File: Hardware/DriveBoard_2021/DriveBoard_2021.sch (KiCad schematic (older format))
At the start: 66 parts, among them SW1 SW_Push, SW2 SW_Push, SW3 SW_Push, SW4 SW_Push, SW5 SW_Push, SW6 SW_Push, U1 TM4C129E_Launchpad, U2 LM2576S-3.3, U3 LM2576HVS-5, U4 MCP2551-I-SN

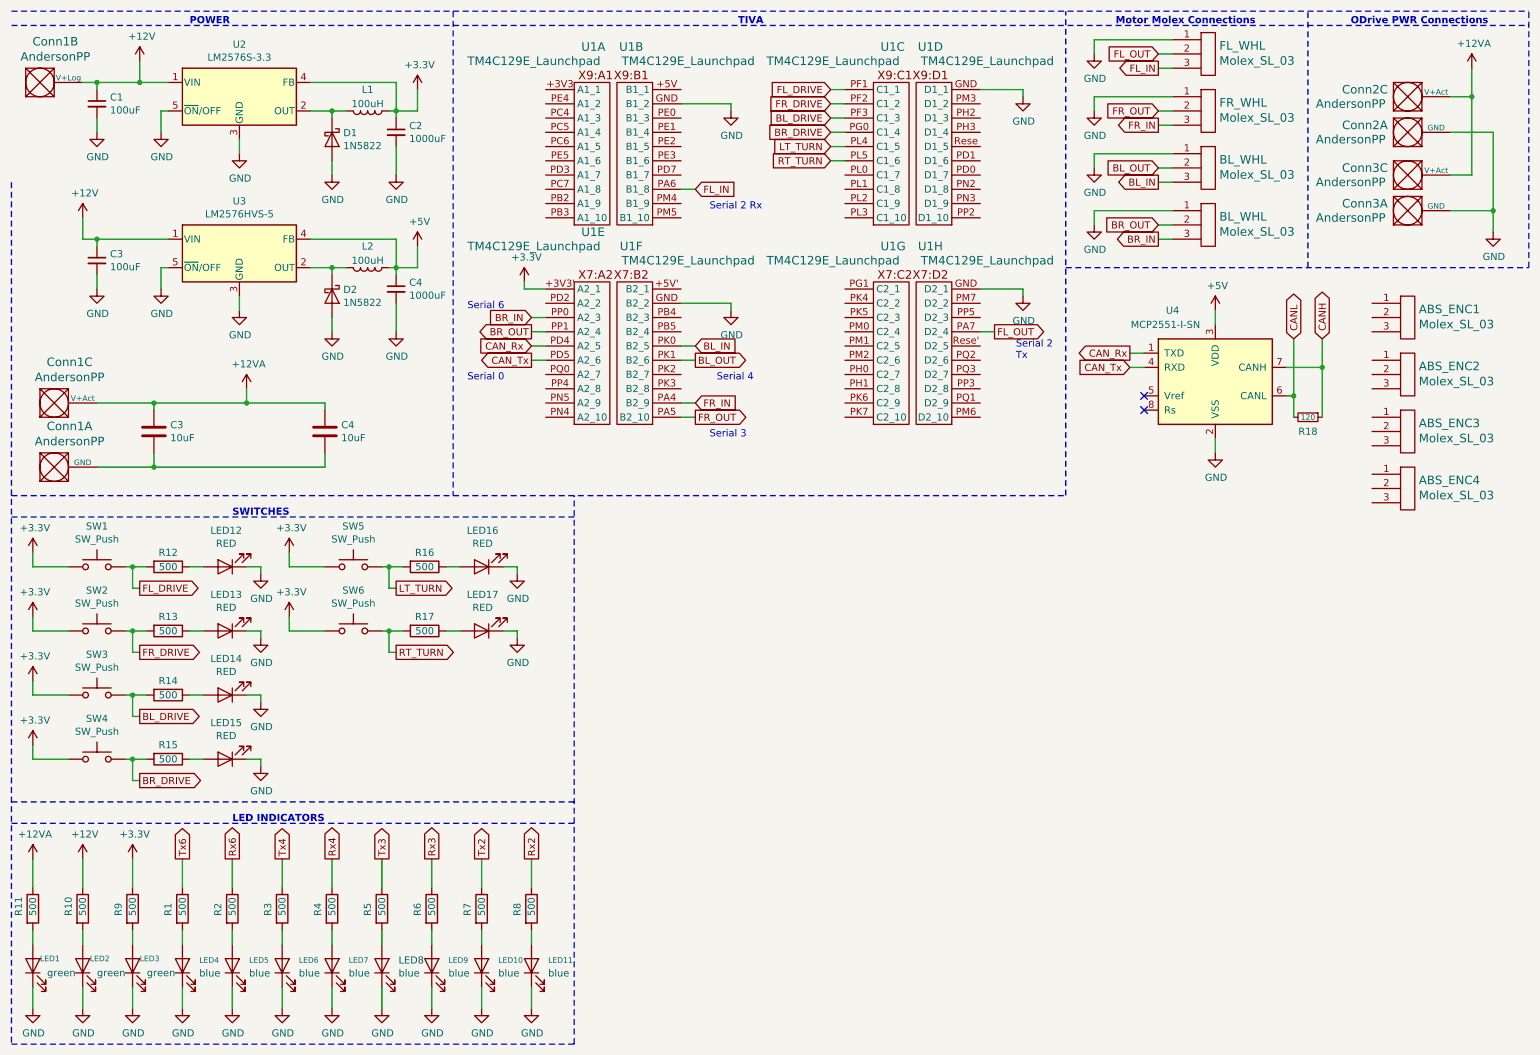
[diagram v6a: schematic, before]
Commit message: Added ODrive Serial, Added LED Indicators, Changed Serial Naming
Changed serial naming for easier understanding of pinout. Added LED indicators for 5V line, CAN serial, and both ODrive serial connections.
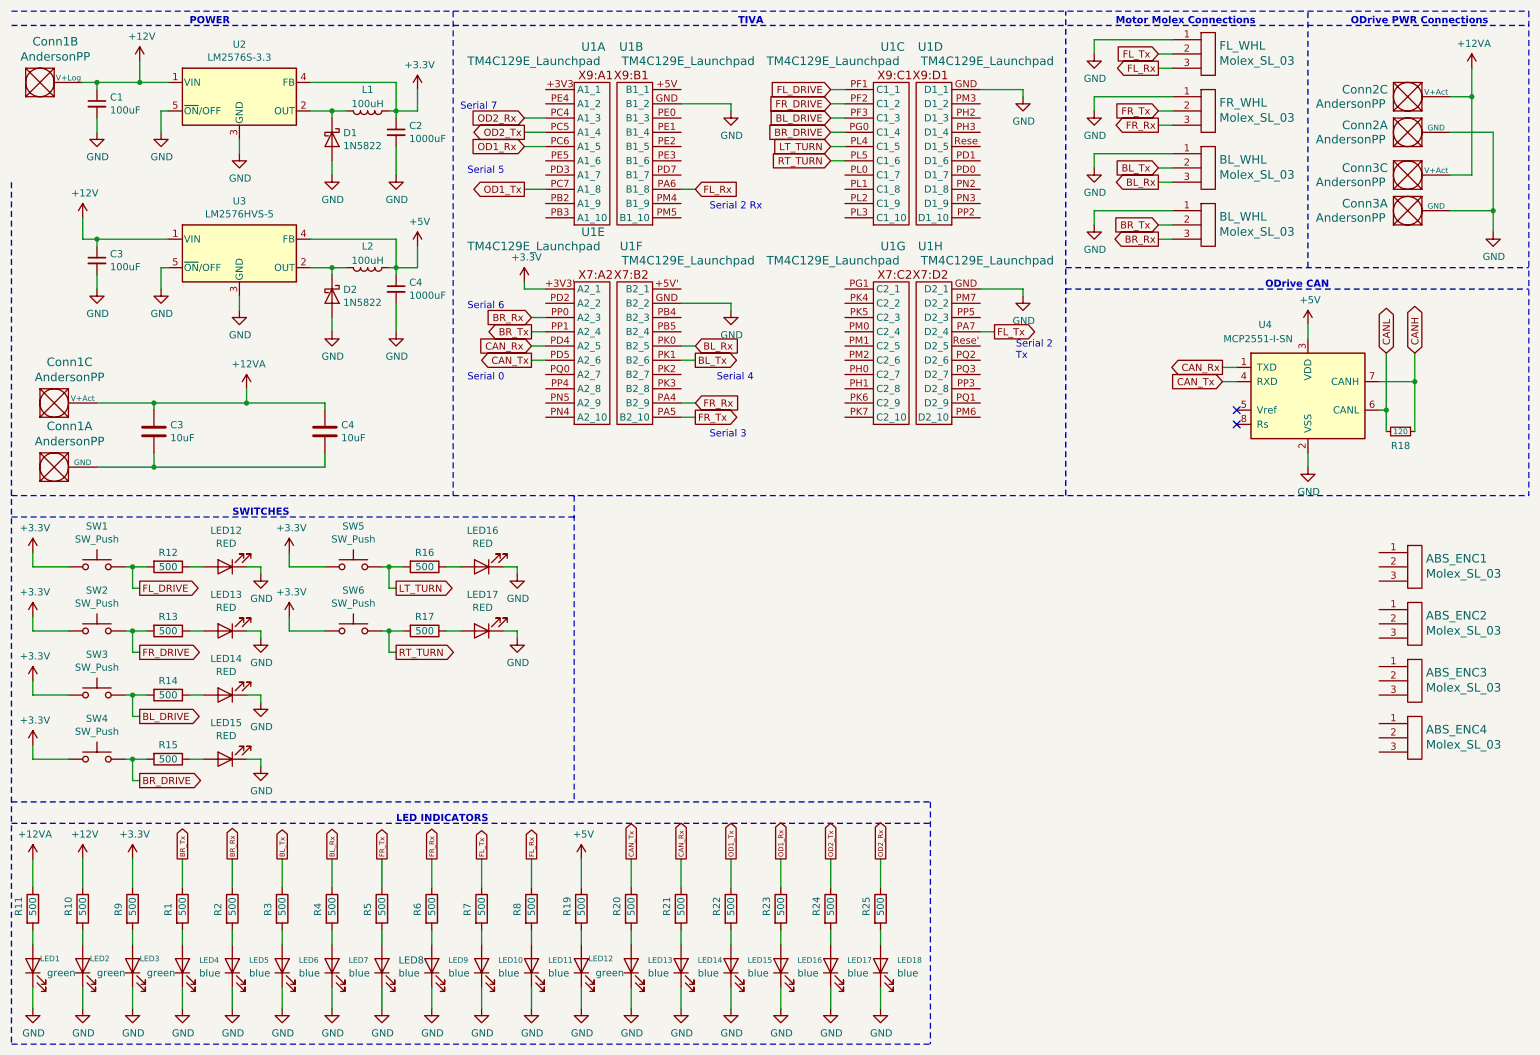
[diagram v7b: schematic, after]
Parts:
- added LED12: green, symbol Device:LED
- added LED13, LED14, LED15, LED16, LED17, LED18: blue, symbol Device:LED
- added R19, R20, R21, R22, R23, R24, R25: 500, symbol Device:R
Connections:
- net Rx2 is gone; now on net FL_Rx: R8.1
- net Rx3 is gone; now on net FR_Rx: R6.1
- net Rx4 is gone; now on net BL_Rx: R4.1
- net Rx6 is gone; now on net BR_Rx: R2.1
- net Tx2 is gone; now on net FL_Tx: R7.1
- net Tx3 is gone; now on net FR_Tx: R5.1
- net Tx4 is gone; now on net BL_Tx: R3.1
- net Tx6 is gone; now on net BR_Tx: R1.1
- net +5V: now also R19.1
- net CAN_Rx: now also R21.1
- net CAN_Tx: now also R20.1
- net GND: now also LED12.1 (K), LED13.1 (K), LED14.1 (K), LED15.1 (K), LED16.1 (K), LED17.1 (K), LED18.1 (K)
- net OD2_Rx: now reaches U1.PC4 (A1_3)
- net OD2_Rx: now also R25.1
- net OD2_Tx: now reaches U1.PC5 (A1_4)
- net OD2_Tx: now also R24.1
- net OD1_Rx: now reaches U1.PC6 (A1_5)
- net OD1_Rx: now also R23.1
- net OD1_Tx: now reaches U1.PC7 (A1_8)
- net OD1_Tx: now also R22.1
- net BL_IN renamed BL_Rx
- net BL_OUT renamed BL_Tx
- net BR_IN renamed BR_Rx
- net BR_OUT renamed BR_Tx
- net FL_IN renamed FL_Rx
- net FL_OUT renamed FL_Tx
- net FR_IN renamed FR_Rx
- net FR_OUT renamed FR_Tx
- new net: LED12.2 (A), R19.2
- new net: LED14.2 (A), R21.2
- new net: LED13.2 (A), R20.2
- new net: LED16.2 (A), R23.2
- new net: LED15.2 (A), R22.2
- new net: LED18.2 (A), R25.2
- new net: LED17.2 (A), R24.2
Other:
- note added: "ODrive CAN"
- note added: "Serial 5\n"
- note added: "Serial 7"
- moved on the sheet: ABS_ENC1, ABS_ENC2, ABS_ENC3, ABS_ENC4, R18, U4

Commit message: Absolute Encoder Connections Added
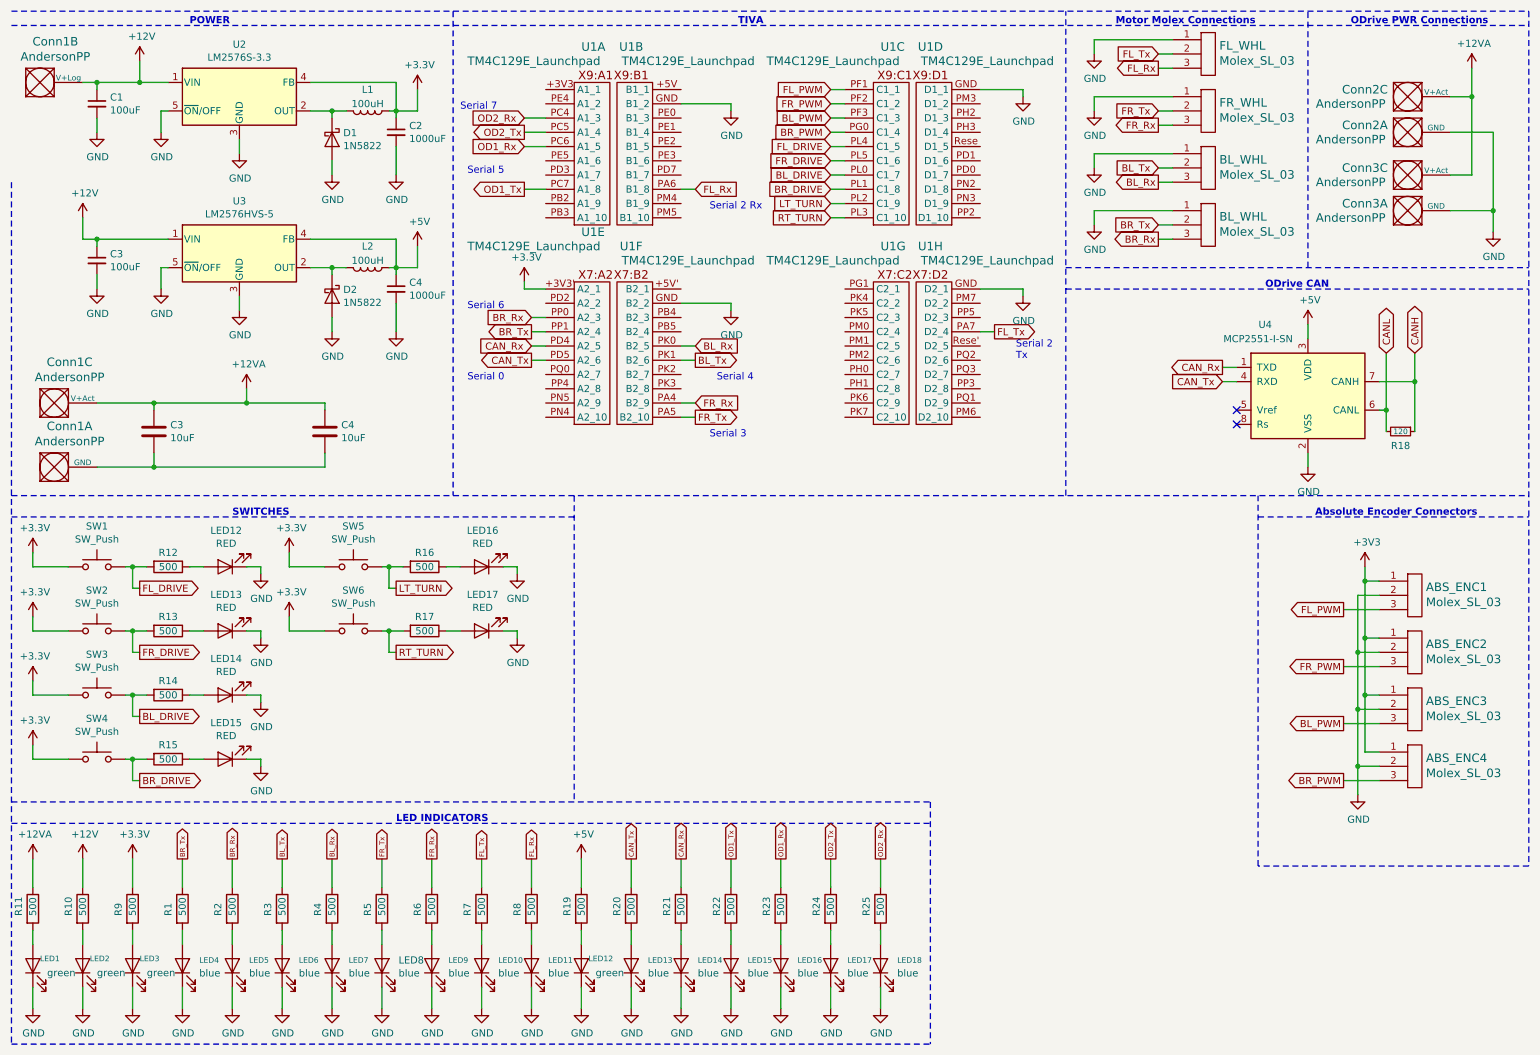
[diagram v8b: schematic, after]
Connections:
- net +3V3: now also ABS_ENC1.1, ABS_ENC2.1, ABS_ENC3.1, ABS_ENC4.1
- net BL_DRIVE: now also U1.PL0 (C1_7); no longer U1.PF3 (C1_3)
- net BR_DRIVE: now also U1.PL1 (C1_8); no longer U1.PG0 (C1_4)
- net FL_DRIVE: now also U1.PL4 (C1_5); no longer U1.PF1 (C1_1)
- net FR_DRIVE: now also U1.PL5 (C1_6); no longer U1.PF2 (C1_2)
- net GND: now also ABS_ENC1.2, ABS_ENC2.2, ABS_ENC3.2, ABS_ENC4.2
- net LT_TURN: now also U1.PL2 (C1_9); no longer U1.PL4 (C1_5)
- net RT_TURN: now also U1.PL3 (C1_10); no longer U1.PL5 (C1_6)
- net FL_PWM: now reaches ABS_ENC1.3
- net FL_PWM: now also U1.PF1 (C1_1)
- net FR_PWM: now reaches ABS_ENC2.3
- net FR_PWM: now also U1.PF2 (C1_2)
- net BL_PWM: now reaches ABS_ENC3.3
- net BL_PWM: now also U1.PF3 (C1_3)
- net BR_PWM: now reaches ABS_ENC4.3
- net BR_PWM: now also U1.PG0 (C1_4)
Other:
- note added: "Absolute Encoder Connectors"
- moved on the sheet: ABS_ENC1, ABS_ENC2, ABS_ENC3, ABS_ENC4
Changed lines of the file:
@@
 Wire Wire Line
 	1350 5900 1350 5750
-Text GLabel 6250 1050 0    50   Input ~ 0
+Text GLabel 6250 1450 0    50   Input ~ 0
 FL_DRIVE
-Text GLabel 6250 1150 0    50   Input ~ 0
+Text GLabel 6250 1550 0    50   Input ~ 0
 FR_DRIVE
-Text GLabel 6250 1250 0    50   Input ~ 0
+Text GLabel 6250 1650 0    50   Input ~ 0
 BL_DRIVE
-Text GLabel 6250 1350 0    50   Input ~ 0
+Text GLabel 6250 1750 0    50   Input ~ 0
 BR_DRIVE
 Wire Wire Line
@@
 Wire Wire Line
 	2450 4750 2450 4850
-Text GLabel 6250 1450 0    50   Input ~ 0
+Text GLabel 6250 1850 0    50   Input ~ 0
 LT_TURN
-Text GLabel 6250 1550 0    50   Input ~ 0
+Text GLabel 6250 1950 0    50   Input ~ 0
 RT_TURN
 Wire Wire Line
@@
 L MRDT_Connectors:Molex_SL_03 ABS_ENC1
 U 1 1 5F7216D7
-P 10300 4550
-F 0 "ABS_ENC1" H 10428 4758 60  0000 L CNN
-F 1 "Molex_SL_03" H 10428 4652 60  0000 L CNN
-F 2 "" H 10300 4550 60  0001 C CNN
-F 3 "" H 10300 4550 60  0001 C CNN
-	1    10300 4550
+P 10300 4750
+F 0 "ABS_ENC1" H 10428 4958 60  0000 L CNN
+F 1 "Molex_SL_03" H 10428 4852 60  0000 L CNN
+F 2 "" H 10300 4750 60  0001 C CNN
+F 3 "" H 10300 4750 60  0001 C CNN
+	1    10300 4750
 	1    0    0    -1
 $EndComp
@@
 L MRDT_Connectors:Molex_SL_03 ABS_ENC2
 U 1 1 5F7216DD
-P 10300 4950
-F 0 "ABS_ENC2" H 10428 5158 60  0000 L CNN
-F 1 "Molex_SL_03" H 10428 5052 60  0000 L CNN
-F 2 "" H 10300 4950 60  0001 C CNN
-F 3 "" H 10300 4950 60  0001 C CNN
-	1    10300 4950
+P 10300 5150
+F 0 "ABS_ENC2" H 10428 5358 60  0000 L CNN
+F 1 "Molex_SL_03" H 10428 5252 60  0000 L CNN
+F 2 "" H 10300 5150 60  0001 C CNN
+F 3 "" H 10300 5150 60  0001 C CNN
+	1    10300 5150
 	1    0    0    -1
 $EndComp
@@
 L MRDT_Connectors:Molex_SL_03 ABS_ENC3
 U 1 1 5F7216E3
-P 10300 5350
-F 0 "ABS_ENC3" H 10428 5558 60  0000 L CNN
-F 1 "Molex_SL_03" H 10428 5452 60  0000 L CNN
-F 2 "" H 10300 5350 60  0001 C CNN
-F 3 "" H 10300 5350 60  0001 C CNN
-	1    10300 5350
+P 10300 5550
+F 0 "ABS_ENC3" H 10428 5758 60  0000 L CNN
+F 1 "Molex_SL_03" H 10428 5652 60  0000 L CNN
+F 2 "" H 10300 5550 60  0001 C CNN
+F 3 "" H 10300 5550 60  0001 C CNN
+	1    10300 5550
 	1    0    0    -1
 $EndComp
@@
 L MRDT_Connectors:Molex_SL_03 ABS_ENC4
 U 1 1 5F7216E9
-P 10300 5750
-F 0 "ABS_ENC4" H 10428 5958 60  0000 L CNN
-F 1 "Molex_SL_03" H 10428 5852 60  0000 L CNN
-F 2 "" H 10300 5750 60  0001 C CNN
-F 3 "" H 10300 5750 60  0001 C CNN
-	1    10300 5750
+P 10300 5950
+F 0 "ABS_ENC4" H 10428 6158 60  0000 L CNN
+F 1 "Molex_SL_03" H 10428 6052 60  0000 L CNN
+F 2 "" H 10300 5950 60  0001 C CNN
+F 3 "" H 10300 5950 60  0001 C CNN
+	1    10300 5950
 	1    0    0    -1
 $EndComp
@@
 Wire Notes Line
 	500  3900 11150 3900
-Wire Notes Line
-	11150 500  11150 3900
 Text Notes 9300 2450 0    50   ~ 10
 ODrive CAN
@@
 Text Notes 3650 1200 0    50   ~ 0
 Serial 7
+$Comp
+L power:+3V3 #PWR?
+U 1 1 5F9F6160
+P 10000 4400
+F 0 "#PWR?" H 10000 4250 50  0001 C CNN
+F 1 "+3V3" H 10015 4573 50  0000 C CNN
+F 2 "" H 10000 4400 50  0001 C CNN
+F 3 "" H 10000 4400 50  0001 C CNN
+	1    10000 4400
+	1    0    0    -1
+$EndComp
+$Comp
+L power:GND #PWR?
+U 1 1 5F9F79C6
+P 9950 6000
+F 0 "#PWR?" H 9950 5750 50  0001 C CNN
+F 1 "GND" H 9955 5827 50  0000 C CNN
+F 2 "" H 9950 6000 50  0001 C CNN
+F 3 "" H 9950 6000 50  0001 C CNN
+	1    9950 6000
+	1    0    0    -1
+$EndComp
+Wire Wire Line
+	10000 4400 10000 4500
+Wire Wire Line
+	10000 4500 10100 4500
+Wire Wire Line
+	10100 4900 10000 4900
+Wire Wire Line
+	10000 4900 10000 4500
+Connection ~ 10000 4500
+Wire Wire Line
+	10100 5300 10000 5300
+Wire Wire Line
+	10000 5300 10000 4900
+Connection ~ 10000 4900
+Wire Wire Line
+	10100 5700 10000 5700
+Wire Wire Line
+	10000 5700 10000 5300
+Connection ~ 10000 5300
+Wire Wire Line
+	9950 6000 9950 5800
+Wire Wire Line
+	9950 5800 10100 5800
+Wire Wire Line
+	10100 5400 9950 5400
+Wire Wire Line
+	9950 5400 9950 5800
+Connection ~ 9950 5800
+Wire Wire Line
+	10100 5000 9950 5000
+Wire Wire Line
+	9950 5000 9950 5400
+Connection ~ 9950 5400
+Wire Wire Line
+	10100 4600 9950 4600
+Wire Wire Line
+	9950 4600 9950 5000
+Connection ~ 9950 5000
+Text GLabel 9850 4700 0    50   Output ~ 0
+FL_PWM
+Text GLabel 9850 5100 0    50   Output ~ 0
+FR_PWM
+Text GLabel 9850 5500 0    50   Output ~ 0
+BL_PWM
+Text GLabel 9850 5900 0    50   Output ~ 0
+BR_PWM
+Wire Wire Line
+	10100 4700 9850 4700
+Wire Wire Line
+	10100 5100 9850 5100
+Wire Wire Line
+	10100 5500 9850 5500
+Wire Wire Line
+	10100 5900 9850 5900
+Wire Notes Line
+	11150 6500 9250 6500
+Wire Notes Line
+	9250 6500 9250 3900
+Wire Notes Line
+	11150 500  11150 6500
+Wire Notes Line
+	9250 4050 11150 4050
+Text Notes 9650 4050 0    50   ~ 10
+Absolute Encoder Connectors
+Wire Wire Line
+	6350 1650 6250 1650
+Wire Wire Line
+	6350 1750 6250 1750
+Wire Wire Line
+	6350 1850 6250 1850
+Wire Wire Line
+	6350 1950 6250 1950
+Text GLabel 6250 1050 0    50   Input ~ 0
+FL_PWM
+Text GLabel 6250 1150 0    50   Input ~ 0
+FR_PWM
+Text GLabel 6250 1250 0    50   Input ~ 0
+BL_PWM
+Text GLabel 6250 1350 0    50   Input ~ 0
+BR_PWM
 $EndSCHEMATC
